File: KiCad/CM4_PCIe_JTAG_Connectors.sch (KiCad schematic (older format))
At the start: 3 parts

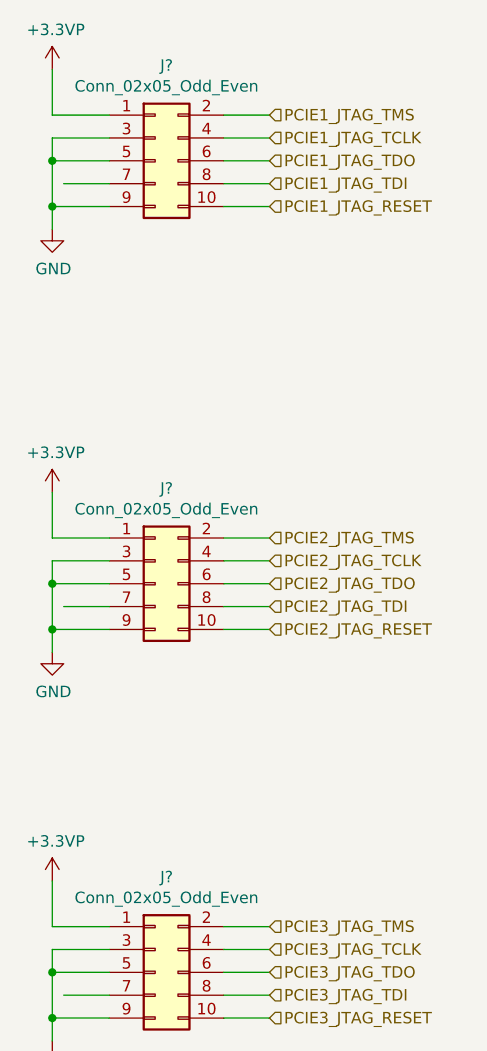
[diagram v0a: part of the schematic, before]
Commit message: updated PCB with RTC circuit
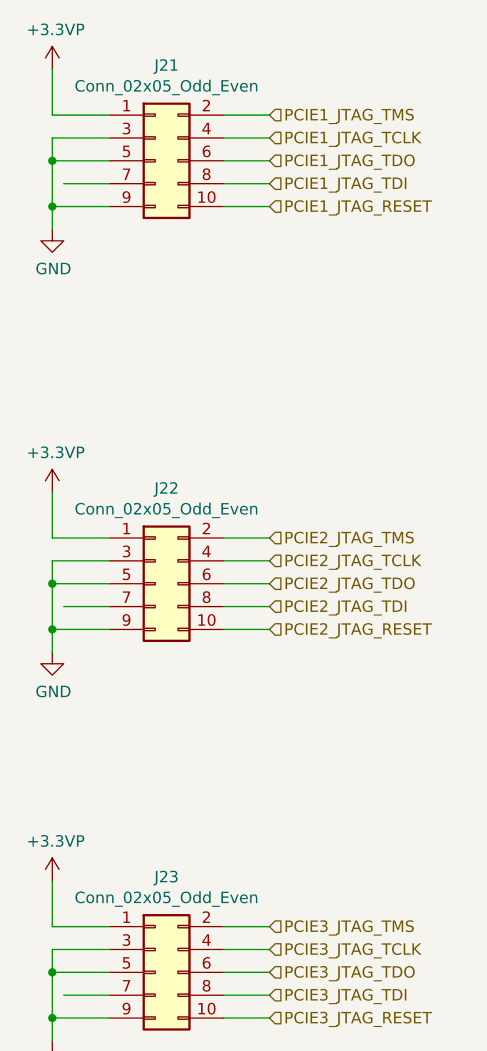
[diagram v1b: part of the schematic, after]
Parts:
- gave numbers to parts that had none: 3
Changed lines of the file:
@@
 $EndDescr
 $Comp
-L Connector_Generic:Conn_02x05_Odd_Even J?
+L Connector_Generic:Conn_02x05_Odd_Even J21
 U 1 1 5FEFA9C8
 P 5700 1450
-F 0 "J?" H 5750 1867 50  0000 C CNN
+F 0 "J21" H 5750 1867 50  0000 C CNN
 F 1 "Conn_02x05_Odd_Even" H 5750 1776 50  0000 C CNN
 F 2 "" H 5700 1450 50  0001 C CNN
@@
 PCIE1_JTAG_RESET
 $Comp
-L Connector_Generic:Conn_02x05_Odd_Even J?
+L Connector_Generic:Conn_02x05_Odd_Even J22
 U 1 1 5FF01F75
 P 5700 3300
-F 0 "J?" H 5750 3717 50  0000 C CNN
+F 0 "J22" H 5750 3717 50  0000 C CNN
 F 1 "Conn_02x05_Odd_Even" H 5750 3626 50  0000 C CNN
 F 2 "" H 5700 3300 50  0001 C CNN
@@
 PCIE2_JTAG_RESET
 $Comp
-L Connector_Generic:Conn_02x05_Odd_Even J?
+L Connector_Generic:Conn_02x05_Odd_Even J23
 U 1 1 5FF02E31
 P 5700 5000
-F 0 "J?" H 5750 5417 50  0000 C CNN
+F 0 "J23" H 5750 5417 50  0000 C CNN
 F 1 "Conn_02x05_Odd_Even" H 5750 5326 50  0000 C CNN
 F 2 "" H 5700 5000 50  0001 C CNN
@@
 	5250 3100 5500 3100
 $Comp
-L CM4_MATX:GND #PWR?
+L CM4_MATX:GND #PWR0214
 U 1 1 5FF1138C
 P 5250 3600
-F 0 "#PWR?" H 5250 3350 50  0001 C CNN
+F 0 "#PWR0214" H 5250 3350 50  0001 C CNN
 F 1 "GND" H 5255 3427 50  0000 C CNN
 F 2 "" H 5250 3600 50  0001 C CNN
@@
 $EndComp
 $Comp
-L CM4_MATX:GND #PWR?
+L CM4_MATX:GND #PWR0215
 U 1 1 5FF116BE
 P 5250 5300
-F 0 "#PWR?" H 5250 5050 50  0001 C CNN
+F 0 "#PWR0215" H 5250 5050 50  0001 C CNN
 F 1 "GND" H 5255 5127 50  0000 C CNN
 F 2 "" H 5250 5300 50  0001 C CNN
@@
 $EndComp
 $Comp
-L CM4_MATX:GND #PWR?
+L CM4_MATX:GND #PWR0216
 U 1 1 5FF119C5
 P 5250 1750
-F 0 "#PWR?" H 5250 1500 50  0001 C CNN
+F 0 "#PWR0216" H 5250 1500 50  0001 C CNN
 F 1 "GND" H 5255 1577 50  0000 C CNN
 F 2 "" H 5250 1750 50  0001 C CNN
@@
 $EndComp
 $Comp
-L power:+3.3VP #PWR?
+L power:+3.3VP #PWR0217
 U 1 1 5FF11C6C
 P 5250 4600
-F 0 "#PWR?" H 5400 4550 50  0001 C CNN
+F 0 "#PWR0217" H 5400 4550 50  0001 C CNN
 F 1 "+3.3VP" H 5265 4773 50  0000 C CNN
 F 2 "" H 5250 4600 50  0001 C CNN
@@
 $EndComp
 $Comp
-L power:+3.3VP #PWR?
+L power:+3.3VP #PWR0218
 U 1 1 5FF12037
 P 5250 2900
-F 0 "#PWR?" H 5400 2850 50  0001 C CNN
+F 0 "#PWR0218" H 5400 2850 50  0001 C CNN
 F 1 "+3.3VP" H 5265 3073 50  0000 C CNN
 F 2 "" H 5250 2900 50  0001 C CNN
@@
 $EndComp
 $Comp
-L power:+3.3VP #PWR?
+L power:+3.3VP #PWR0219
 U 1 1 5FF122A9
 P 5250 1050
-F 0 "#PWR?" H 5400 1000 50  0001 C CNN
+F 0 "#PWR0219" H 5400 1000 50  0001 C CNN
 F 1 "+3.3VP" H 5265 1223 50  0000 C CNN
 F 2 "" H 5250 1050 50  0001 C CNN

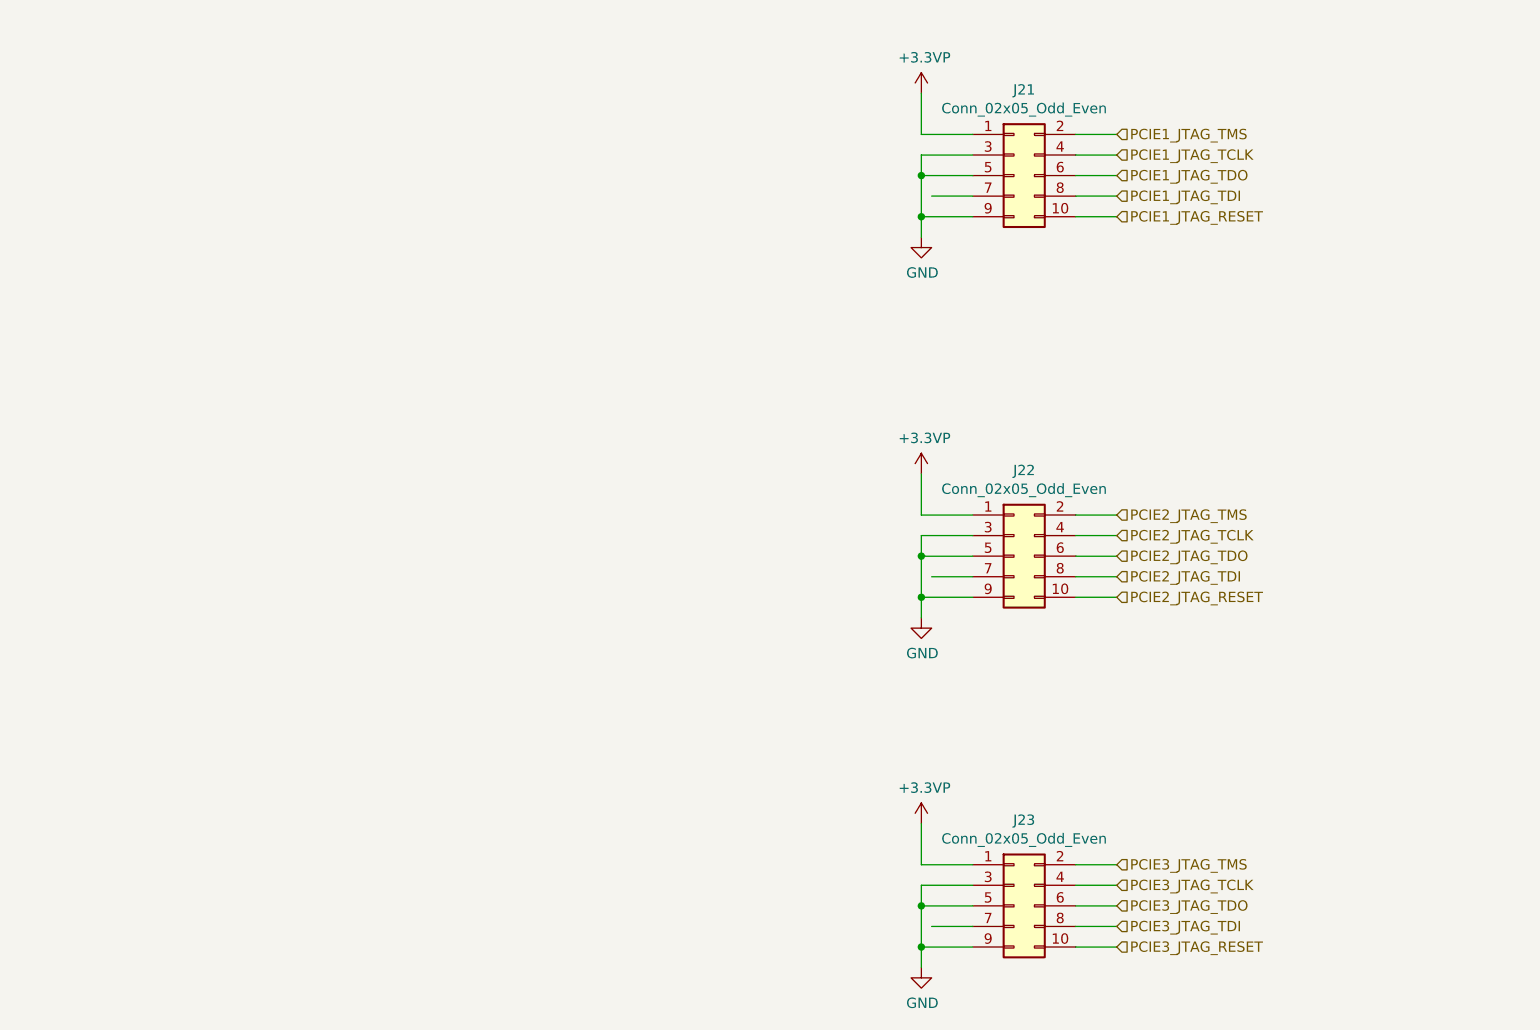
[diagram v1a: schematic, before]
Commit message: Tons of wiring and pin straps for PCI-e Switch
Also re-did some hierarchical labels for JTAG
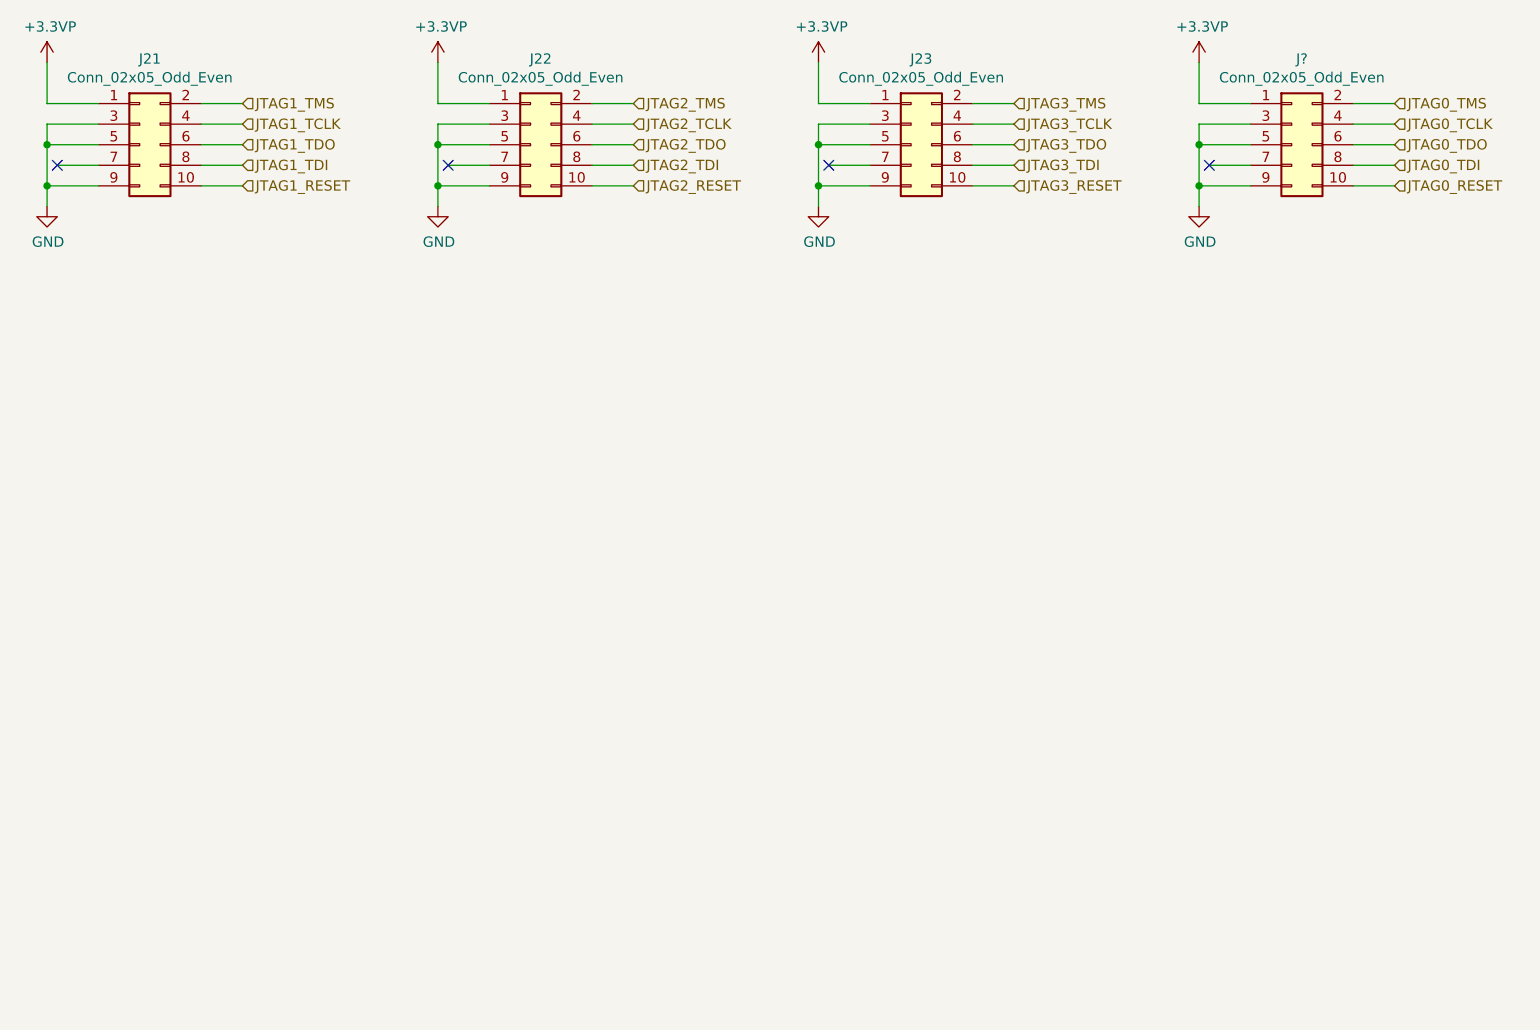
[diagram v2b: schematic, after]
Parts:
- added J?: Conn_02x05_Odd_Even, symbol Connector_Generic:Conn_02x05_Odd_Even
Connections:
- net labels added: JTAG0_RESET, JTAG0_TCLK, JTAG0_TDI, JTAG0_TDO, JTAG0_TMS, JTAG1_RESET, JTAG1_TCLK, JTAG1_TDI, JTAG1_TDO, JTAG1_TMS, JTAG2_RESET, JTAG2_TCLK, JTAG2_TDI, JTAG2_TDO, JTAG2_TMS, JTAG3_RESET, JTAG3_TCLK, JTAG3_TDI, JTAG3_TDO, JTAG3_TMS
- net labels removed: PCIE1_JTAG_RESET, PCIE1_JTAG_TCLK, PCIE1_JTAG_TDI, PCIE1_JTAG_TDO, PCIE1_JTAG_TMS, PCIE2_JTAG_RESET, PCIE2_JTAG_TCLK, PCIE2_JTAG_TDI, PCIE2_JTAG_TDO, PCIE2_JTAG_TMS, PCIE3_JTAG_RESET, PCIE3_JTAG_TCLK, PCIE3_JTAG_TDI, PCIE3_JTAG_TDO, PCIE3_JTAG_TMS
- wire segments 42 -> 56
- no-connect marks 0 -> 4
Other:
- moved on the sheet: J21, J22, J23

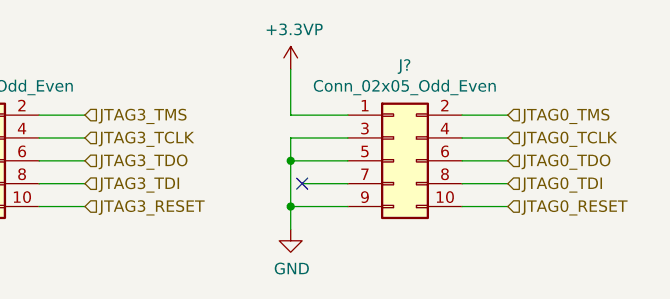
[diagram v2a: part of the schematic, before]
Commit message: Added second USB dual-stack header and fixed some library references.
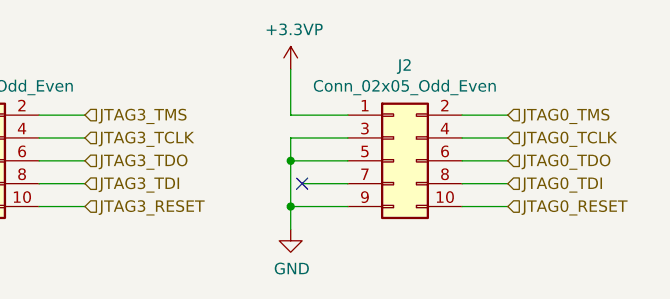
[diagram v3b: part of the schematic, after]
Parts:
- gave numbers to parts that had none: 1
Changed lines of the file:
@@
 $EndComp
 $Comp
-L Connector_Generic:Conn_02x05_Odd_Even J?
+L Connector_Generic:Conn_02x05_Odd_Even J2
 U 1 1 61951787
 P 7050 1300
-F 0 "J?" H 7100 1717 50  0000 C CNN
+F 0 "J2" H 7100 1717 50  0000 C CNN
 F 1 "Conn_02x05_Odd_Even" H 7100 1626 50  0000 C CNN
 F 2 "" H 7050 1300 50  0001 C CNN
@@
 	7350 1500 7550 1500
 $Comp
-L power:+3.3VP #PWR?
+L power:+3.3VP #PWR0230
 U 1 1 6195736D
 P 6600 900
-F 0 "#PWR?" H 6750 850 50  0001 C CNN
+F 0 "#PWR0230" H 6750 850 50  0001 C CNN
 F 1 "+3.3VP" H 6615 1073 50  0000 C CNN
 F 2 "" H 6600 900 50  0001 C CNN
@@
 	6600 1200 6850 1200
 $Comp
-L CM4_MATX:GND #PWR?
+L CM4_MATX:GND #PWR0231
 U 1 1 619593B4
 P 6600 1600
-F 0 "#PWR?" H 6600 1350 50  0001 C CNN
+F 0 "#PWR0231" H 6600 1350 50  0001 C CNN
 F 1 "GND" H 6605 1427 50  0000 C CNN
 F 2 "" H 6600 1600 50  0001 C CNN

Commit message: Updated CM4 footprints/symbols, mounting holes
This is in a bid to make it more manufactuerable by reducing the need for explanations and questions.
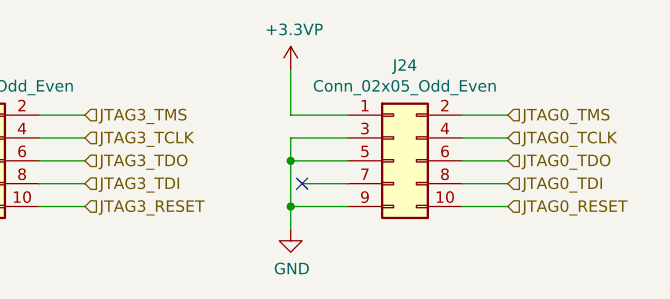
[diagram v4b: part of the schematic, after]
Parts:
- renumbered J2 to J24
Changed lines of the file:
@@
 Sheet 15 16
 Title ""
-Date ""
+Date "2021-02-08"
 Rev ""
 Comp ""
@@
 $EndComp
 $Comp
-L Connector_Generic:Conn_02x05_Odd_Even J2
+L Connector_Generic:Conn_02x05_Odd_Even J24
 U 1 1 61951787
 P 7050 1300
-F 0 "J2" H 7100 1717 50  0000 C CNN
+F 0 "J24" H 7100 1717 50  0000 C CNN
 F 1 "Conn_02x05_Odd_Even" H 7100 1626 50  0000 C CNN
 F 2 "" H 7050 1300 50  0001 C CNN

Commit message: Started picking passive components, overhauled library
Cleaned up a bunch of schematic library references.
Added datasheets, descriptions for a lot of existing parts.
Picked most capacitor parts, still a couple left.
Cleaned up a fair few footprint references.
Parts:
- J21, J22, J23, J24: footprint (none) -> CM4_MATX:PinHeader_2x05_P2.54mm_Vertical; symbol Connector_Generic:Conn_02x05_Odd_Even -> CM4_MATX:Conn_02x05_Odd_Even; Description (none) -> Standard 2.54mm (100mil)-separated pins
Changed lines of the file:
@@
 $Descr A4 11693 8268
 encoding utf-8
-Sheet 15 16
+Sheet 11 16
 Title ""
 Date "2021-02-08"
@@
 $EndDescr
 $Comp
-L Connector_Generic:Conn_02x05_Odd_Even J21
+L CM4_MATX:Conn_02x05_Odd_Even J21
 U 1 1 5FEFA9C8
 P 1450 1300
 F 0 "J21" H 1500 1717 50  0000 C CNN
 F 1 "Conn_02x05_Odd_Even" H 1500 1626 50  0000 C CNN
-F 2 "" H 1450 1300 50  0001 C CNN
+F 2 "CM4_MATX:PinHeader_2x05_P2.54mm_Vertical" H 1450 1300 50  0001 C CNN
 F 3 "~" H 1450 1300 50  0001 C CNN
+F 4 "Standard 2.54mm (100mil)-separated pins" H 1450 1300 50  0001 C CNN "Description"
 	1    1450 1300
 	1    0    0    -1
@@
 JTAG1_RESET
 $Comp
-L Connector_Generic:Conn_02x05_Odd_Even J22
+L CM4_MATX:Conn_02x05_Odd_Even J22
 U 1 1 5FF01F75
 P 3350 1300
 F 0 "J22" H 3400 1717 50  0000 C CNN
 F 1 "Conn_02x05_Odd_Even" H 3400 1626 50  0000 C CNN
-F 2 "" H 3350 1300 50  0001 C CNN
+F 2 "CM4_MATX:PinHeader_2x05_P2.54mm_Vertical" H 3350 1300 50  0001 C CNN
 F 3 "~" H 3350 1300 50  0001 C CNN
+F 4 "Standard 2.54mm (100mil)-separated pins" H 3350 1300 50  0001 C CNN "Description"
 	1    3350 1300
 	1    0    0    -1
@@
 JTAG2_RESET
 $Comp
-L Connector_Generic:Conn_02x05_Odd_Even J23
+L CM4_MATX:Conn_02x05_Odd_Even J23
 U 1 1 5FF02E31
 P 5200 1300
 F 0 "J23" H 5250 1717 50  0000 C CNN
 F 1 "Conn_02x05_Odd_Even" H 5250 1626 50  0000 C CNN
-F 2 "" H 5200 1300 50  0001 C CNN
+F 2 "CM4_MATX:PinHeader_2x05_P2.54mm_Vertical" H 5200 1300 50  0001 C CNN
 F 3 "~" H 5200 1300 50  0001 C CNN
+F 4 "Standard 2.54mm (100mil)-separated pins" H 5200 1300 50  0001 C CNN "Description"
 	1    5200 1300
 	1    0    0    -1
@@
 $EndComp
 $Comp
-L power:+3.3VP #PWR0217
+L CM4_MATX:+3.3VP #PWR0217
 U 1 1 5FF11C6C
 P 4750 900
@@
 $EndComp
 $Comp
-L power:+3.3VP #PWR0218
+L CM4_MATX:+3.3VP #PWR0218
 U 1 1 5FF12037
 P 2900 900
@@
 $EndComp
 $Comp
-L power:+3.3VP #PWR0219
+L CM4_MATX:+3.3VP #PWR0219
 U 1 1 5FF122A9
 P 1000 900
@@
 $EndComp
 $Comp
-L Connector_Generic:Conn_02x05_Odd_Even J24
+L CM4_MATX:Conn_02x05_Odd_Even J24
 U 1 1 61951787
 P 7050 1300
 F 0 "J24" H 7100 1717 50  0000 C CNN
 F 1 "Conn_02x05_Odd_Even" H 7100 1626 50  0000 C CNN
-F 2 "" H 7050 1300 50  0001 C CNN
+F 2 "CM4_MATX:PinHeader_2x05_P2.54mm_Vertical" H 7050 1300 50  0001 C CNN
 F 3 "~" H 7050 1300 50  0001 C CNN
+F 4 "Standard 2.54mm (100mil)-separated pins" H 7050 1300 50  0001 C CNN "Description"
 	1    7050 1300
 	1    0    0    -1
@@
 	7350 1500 7550 1500
 $Comp
-L power:+3.3VP #PWR0230
+L CM4_MATX:+3.3VP #PWR0230
 U 1 1 6195736D
 P 6600 900

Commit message: Imported new components to the PCB and moved some components
Updated PDFs and added two new board layers. One for ground and a second for power (voltage to be decided)
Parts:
- removed J21, J22, J23, J24: Conn_02x05_Odd_Even, CM4_MATX:PinHeader_2x05_P2.54mm_Vertical, symbol CM4_MATX:Conn_02x05_Odd_Even
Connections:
- no-connect marks 4 -> 0
